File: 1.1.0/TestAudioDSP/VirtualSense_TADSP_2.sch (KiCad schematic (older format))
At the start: 2 parts

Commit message: schematics of audio DSP test layer OK, added module on audio DSP test layer brd
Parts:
- added C24, C26, C30: 100n, symbol CSMALL
- added C25: 1u, symbol CSMALL
- added C27, C28: 33p, symbol CSMALL
- added C29: 10u, symbol CP1SMALL
- added D1: LED, symbol LED
- added P10: DSP-SDA, symbol CONN_1
- added P11: DSP-SCL, symbol CONN_1
- added R16: 220, symbol RSML
- added R17, R19, R21, R22, R23, R24, R26, R27, R28: 10K, symbol RSML
- added R18, R20: 100K, symbol RSML
- added R25: NO, symbol RSML
- added U7: MICRO_SD, symbol MICRO_SD
- added X1: 32.768KHz, symbol QUARZO_2PIN
- U6: renamed from U???; value MICRO_SD -> SD
- gave numbers to parts that had none: 1
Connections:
- net labels added: 3V3, CPU_CLK_12MHZ, DIO1/P7.5, GNDPWR, I2C_SCL, I2C_SDA, I2S2_CLK, I2S2_DX, I2S2_FS, I2S2_RX, RXD/MISO/P2.2/P3.5, SD_CLK, SD_CMD, SD_DATA0, SD_DATA1, SD_DATA2, SD_DATA3, TARGET_PWR_GOOD, TXD/MOSI/P2.1/P3.4, VCC_1V3
- wire segments 0 -> 106
- no-connect marks 0 -> 41
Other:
- moved on the sheet: U5A, U6

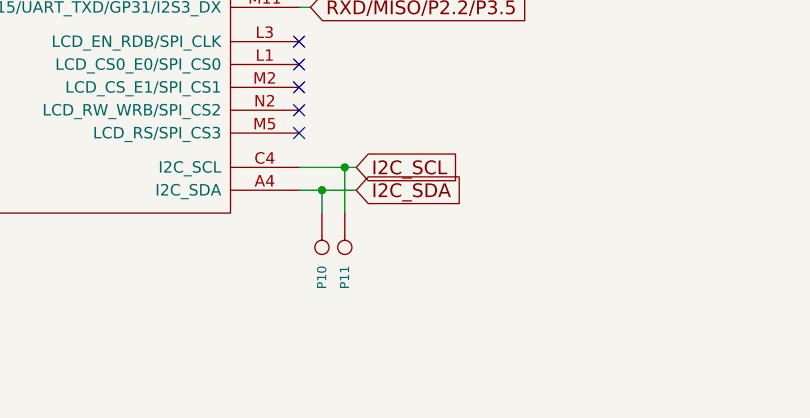
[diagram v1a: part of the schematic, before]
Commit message: audio DSP test layer: brd OK, gerber Ok - sent to PCBoards for check
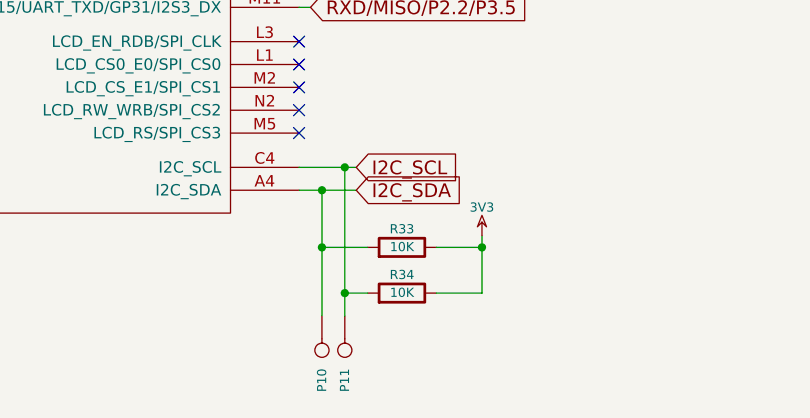
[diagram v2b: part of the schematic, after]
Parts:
- added R33, R34: 10K, symbol RSML
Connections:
- wire segments 106 -> 111
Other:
- moved on the sheet: P10, P11
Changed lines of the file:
@@
 $EndComp
 $Comp
-L GNDPWR #PWR026
+L GNDPWR #PWR38
 U 1 1 521E1491
 P 8650 4450
-F 0 "#PWR026" H 8650 4500 40  0001 C CNN
+F 0 "#PWR38" H 8650 4500 40  0001 C CNN
 F 1 "GNDPWR" H 8650 4370 40  0000 C CNN
 F 2 "" H 8650 4450 60  0001 C CNN
@@
 $EndComp
 $Comp
-L 3V3 #PWR027
+L 3V3 #PWR37
 U 1 1 521E1504
 P 8600 700
-F 0 "#PWR027" H 8600 800 40  0001 C CNN
+F 0 "#PWR37" H 8600 800 40  0001 C CNN
 F 1 "3V3" H 8600 825 40  0000 C CNN
 F 2 "" H 8600 700 60  0001 C CNN
@@
 $EndComp
 $Comp
-L GNDPWR #PWR028
+L GNDPWR #PWR39
 U 1 1 521E1538
 P 8850 1050
-F 0 "#PWR028" H 8850 1100 40  0001 C CNN
+F 0 "#PWR39" H 8850 1100 40  0001 C CNN
 F 1 "GNDPWR" H 8850 970 40  0000 C CNN
 F 2 "" H 8850 1050 60  0001 C CNN
@@
 $EndComp
 $Comp
-L GNDPWR #PWR029
+L GNDPWR #PWR35
 U 1 1 521E2014
 P 5450 2150
-F 0 "#PWR029" H 5450 2200 40  0001 C CNN
+F 0 "#PWR35" H 5450 2200 40  0001 C CNN
 F 1 "GNDPWR" H 5450 2070 40  0000 C CNN
 F 2 "" H 5450 2150 60  0001 C CNN
@@
 $EndComp
 $Comp
-L GNDPWR #PWR030
+L GNDPWR #PWR34
 U 1 1 521E21F5
 P 5350 1550
-F 0 "#PWR030" H 5350 1600 40  0001 C CNN
+F 0 "#PWR34" H 5350 1600 40  0001 C CNN
 F 1 "GNDPWR" H 5350 1470 40  0000 C CNN
 F 2 "" H 5350 1550 60  0001 C CNN
@@
 NoConn ~ 1900 1850
 $Comp
-L GNDPWR #PWR031
+L GNDPWR #PWR31
 U 1 1 521E22FA
 P 1600 1800
-F 0 "#PWR031" H 1600 1850 40  0001 C CNN
+F 0 "#PWR31" H 1600 1850 40  0001 C CNN
 F 1 "GNDPWR" H 1600 1720 40  0000 C CNN
 F 2 "" H 1600 1800 60  0001 C CNN
@@
 $EndComp
 $Comp
-L GNDPWR #PWR032
+L GNDPWR #PWR29
 U 1 1 521E27C4
 P 1300 6900
-F 0 "#PWR032" H 1300 6950 40  0001 C CNN
+F 0 "#PWR29" H 1300 6950 40  0001 C CNN
 F 1 "GNDPWR" H 1300 6820 40  0000 C CNN
 F 2 "" H 1300 6900 60  0001 C CNN
@@
 $EndComp
 $Comp
-L 3V3 #PWR033
+L 3V3 #PWR30
 U 1 1 521E2923
 P 1450 5700
-F 0 "#PWR033" H 1450 5800 40  0001 C CNN
+F 0 "#PWR30" H 1450 5800 40  0001 C CNN
 F 1 "3V3" H 1450 5825 40  0000 C CNN
 F 2 "" H 1450 5700 60  0001 C CNN
@@
 $EndComp
 $Comp
-L GNDPWR #PWR034
+L GNDPWR #PWR33
 U 1 1 521E2CF9
 P 1850 5900
-F 0 "#PWR034" H 1850 5950 40  0001 C CNN
+F 0 "#PWR33" H 1850 5950 40  0001 C CNN
 F 1 "GNDPWR" H 1850 5820 40  0000 C CNN
 F 2 "" H 1850 5900 60  0001 C CNN
@@
 Connection ~ 1250 5250
 $Comp
-L GNDPWR #PWR035
+L GNDPWR #PWR28
 U 1 1 521E2F5E
 P 1250 5650
-F 0 "#PWR035" H 1250 5700 40  0001 C CNN
+F 0 "#PWR28" H 1250 5700 40  0001 C CNN
 F 1 "GNDPWR" H 1250 5570 40  0000 C CNN
 F 2 "" H 1250 5650 60  0001 C CNN
@@
 $EndComp
 $Comp
-L 3V3 #PWR036
+L 3V3 #PWR26
 U 1 1 521E31D9
 P 850 4750
-F 0 "#PWR036" H 850 4850 40  0001 C CNN
+F 0 "#PWR26" H 850 4850 40  0001 C CNN
 F 1 "3V3" H 850 4875 40  0000 C CNN
 F 2 "" H 850 4750 60  0001 C CNN
@@
 $EndComp
 $Comp
-L GNDPWR #PWR037
+L GNDPWR #PWR27
 U 1 1 521E31DF
 P 850 5050
-F 0 "#PWR037" H 850 5100 40  0001 C CNN
+F 0 "#PWR27" H 850 5100 40  0001 C CNN
 F 1 "GNDPWR" H 850 4970 40  0000 C CNN
 F 2 "" H 850 5050 60  0001 C CNN
@@
 NoConn ~ 1900 4850
 $Comp
-L GNDPWR #PWR038
+L GNDPWR #PWR32
 U 1 1 521E336E
 P 1650 4300
-F 0 "#PWR038" H 1650 4350 40  0001 C CNN
+F 0 "#PWR32" H 1650 4350 40  0001 C CNN
 F 1 "GNDPWR" H 1650 4220 40  0000 C CNN
 F 2 "" H 1650 4300 60  0001 C CNN
@@
 L CONN_1 P11
 U 1 1 521F5C97
-P 5350 6600
-F 0 "P11" H 5430 6600 40  0000 L CNN
-F 1 "DSP-SCL" H 5350 6655 30  0001 C CNN
-F 2 "" H 5350 6600 60  0000 C CNN
-F 3 "" H 5350 6600 60  0000 C CNN
-	1    5350 6600
+P 5350 7050
+F 0 "P11" H 5430 7050 40  0000 L CNN
+F 1 "DSP-SCL" H 5350 7105 30  0001 C CNN
+F 2 "" H 5350 7050 60  0000 C CNN
+F 3 "" H 5350 7050 60  0000 C CNN
+	1    5350 7050
 	0    1    1    0
 $EndComp
@@
 L CONN_1 P10
 U 1 1 521F5CA6
-P 5250 6600
-F 0 "P10" H 5330 6600 40  0000 L CNN
-F 1 "DSP-SDA" H 5250 6655 30  0001 C CNN
-F 2 "" H 5250 6600 60  0000 C CNN
-F 3 "" H 5250 6600 60  0000 C CNN
-	1    5250 6600
+P 5250 7050
+F 0 "P10" H 5330 7050 40  0000 L CNN
+F 1 "DSP-SDA" H 5250 7105 30  0001 C CNN
+F 2 "" H 5250 7050 60  0000 C CNN
+F 3 "" H 5250 7050 60  0000 C CNN
+	1    5250 7050
 	0    1    1    0
 $EndComp
 Wire Wire Line
-	5350 6450 5350 6250
+	5350 6250 5350 6900
 Connection ~ 5350 6250
 Wire Wire Line
-	5250 6450 5250 6350
+	5250 6350 5250 6900
 Connection ~ 5250 6350
+$Comp
+L RSML R33
+U 1 1 522054C7
+P 5600 6600
+F 0 "R33" V 5680 6600 40  0000 C CNN
+F 1 "10K" V 5602 6600 40  0000 C CNN
+F 2 "" V 5530 6600 30  0000 C CNN
+F 3 "" H 5600 6600 30  0000 C CNN
+	1    5600 6600
+	0    -1   -1   0
+$EndComp
+$Comp
+L RSML R34
+U 1 1 522054CD
+P 5600 6800
+F 0 "R34" V 5680 6800 40  0000 C CNN
+F 1 "10K" V 5602 6800 40  0000 C CNN
+F 2 "" V 5530 6800 30  0000 C CNN
+F 3 "" H 5600 6800 30  0000 C CNN
+	1    5600 6800
+	0    -1   -1   0
+$EndComp
+Wire Wire Line
+	5450 6800 5350 6800
+Connection ~ 5350 6800
+Wire Wire Line
+	5450 6600 5250 6600
+Connection ~ 5250 6600
+$Comp
+L 3V3 #PWR36
+U 1 1 522056F5
+P 5950 6550
+F 0 "#PWR36" H 5950 6650 40  0001 C CNN
+F 1 "3V3" H 5950 6675 40  0000 C CNN
+F 2 "" H 5950 6550 60  0001 C CNN
+F 3 "" H 5950 6550 60  0001 C CNN
+	1    5950 6550
+	1    0    0    -1
+$EndComp
+Wire Wire Line
+	5950 6550 5950 6800
+Wire Wire Line
+	5950 6800 5750 6800
+Wire Wire Line
+	5750 6600 5950 6600
+Connection ~ 5950 6600
 $EndSCHEMATC

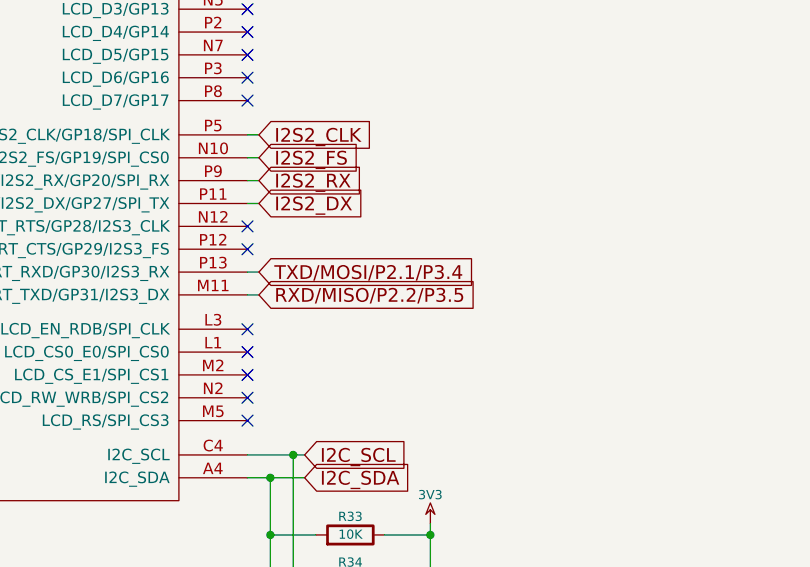
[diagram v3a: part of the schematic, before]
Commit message: audio DSP test layer: changed connection ports CONN2 and CONN4, changed uart port to UART2, changed microphone footprint for edge mounting, schematic OK, brd OK, gerber OK - sent to PCBoards for check
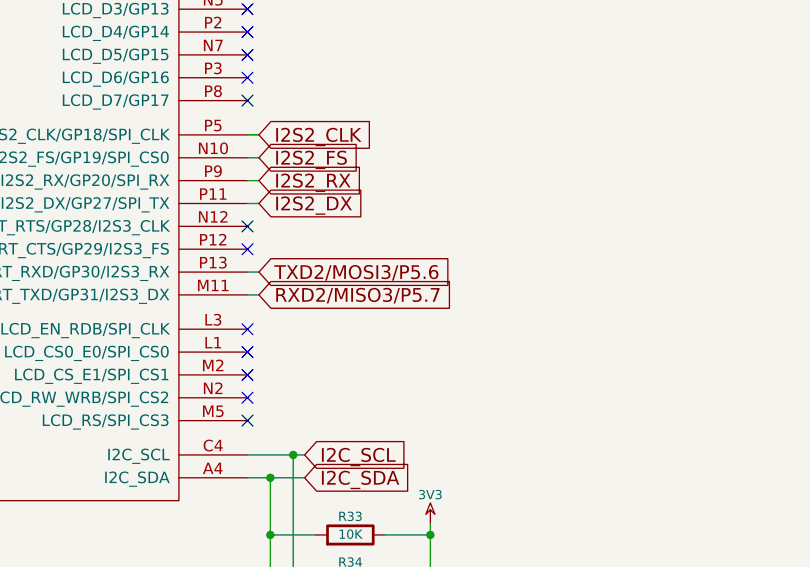
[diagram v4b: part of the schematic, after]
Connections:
- net labels added: RXD2/MISO3/P5.7, TXD2/MOSI3/P5.6
- net labels removed: RXD/MISO/P2.2/P3.5, TXD/MOSI/P2.1/P3.4
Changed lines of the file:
@@
 NoConn ~ 5150 5350
 Text GLabel 5200 5450 2    60   Input ~ 0
-TXD/MOSI/P2.1/P3.4
+TXD2/MOSI3/P5.6
 Text GLabel 5200 5550 2    60   Input ~ 0
-RXD/MISO/P2.2/P3.5
+RXD2/MISO3/P5.7
 NoConn ~ 5150 4700
 NoConn ~ 5150 4600
